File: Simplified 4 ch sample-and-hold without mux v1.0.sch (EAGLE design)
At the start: 8 parts, among them IC5 TL074JT

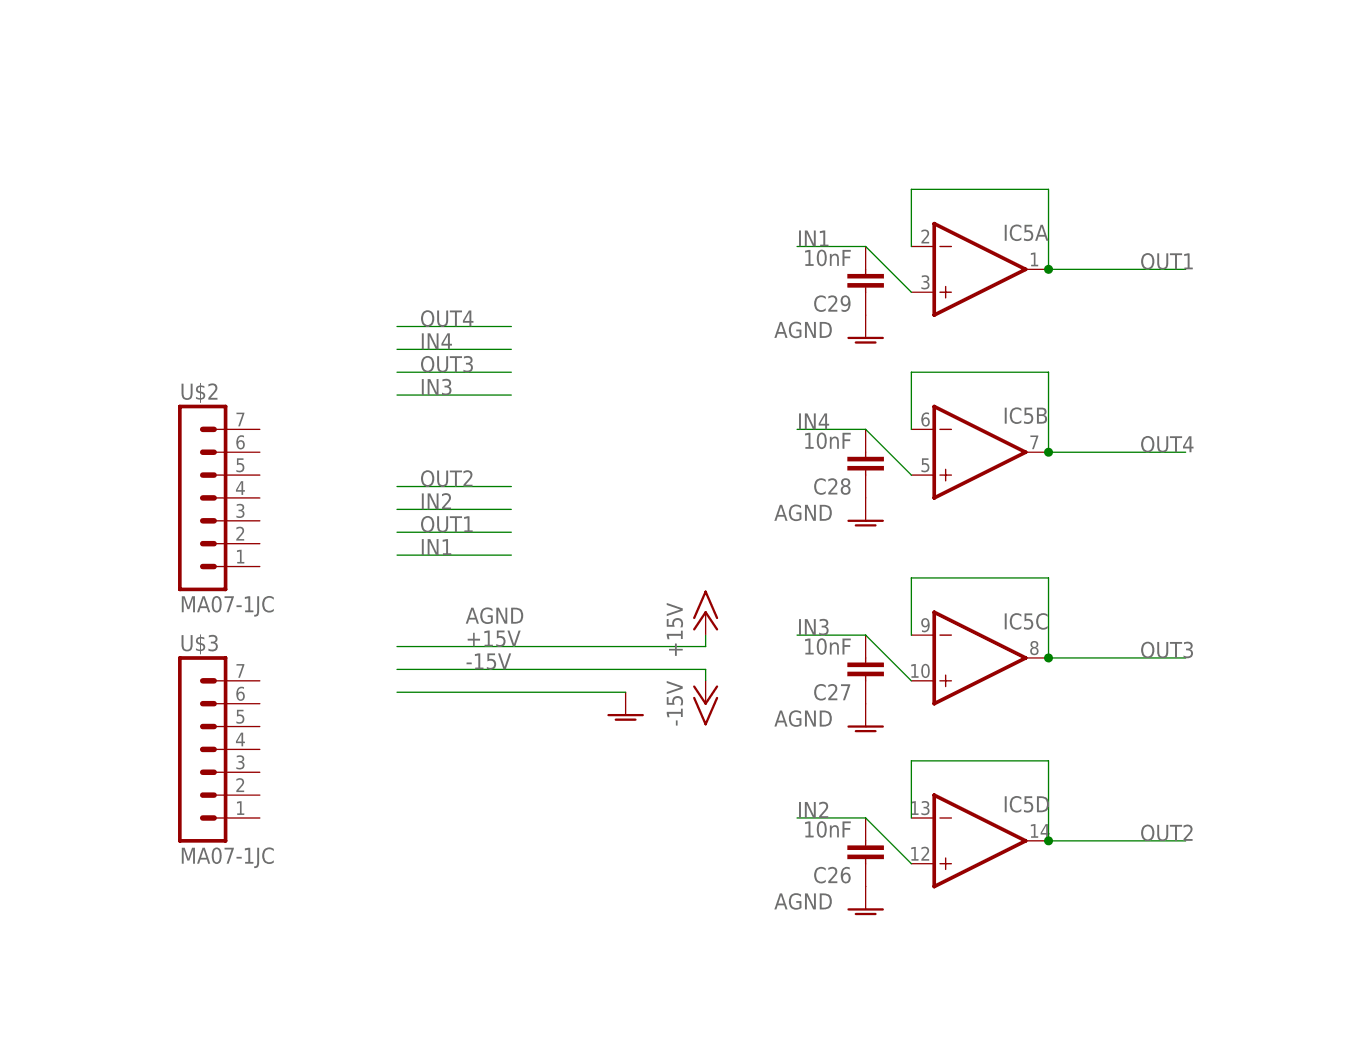
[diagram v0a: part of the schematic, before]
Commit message: Almost completed simplified 4ch s & h
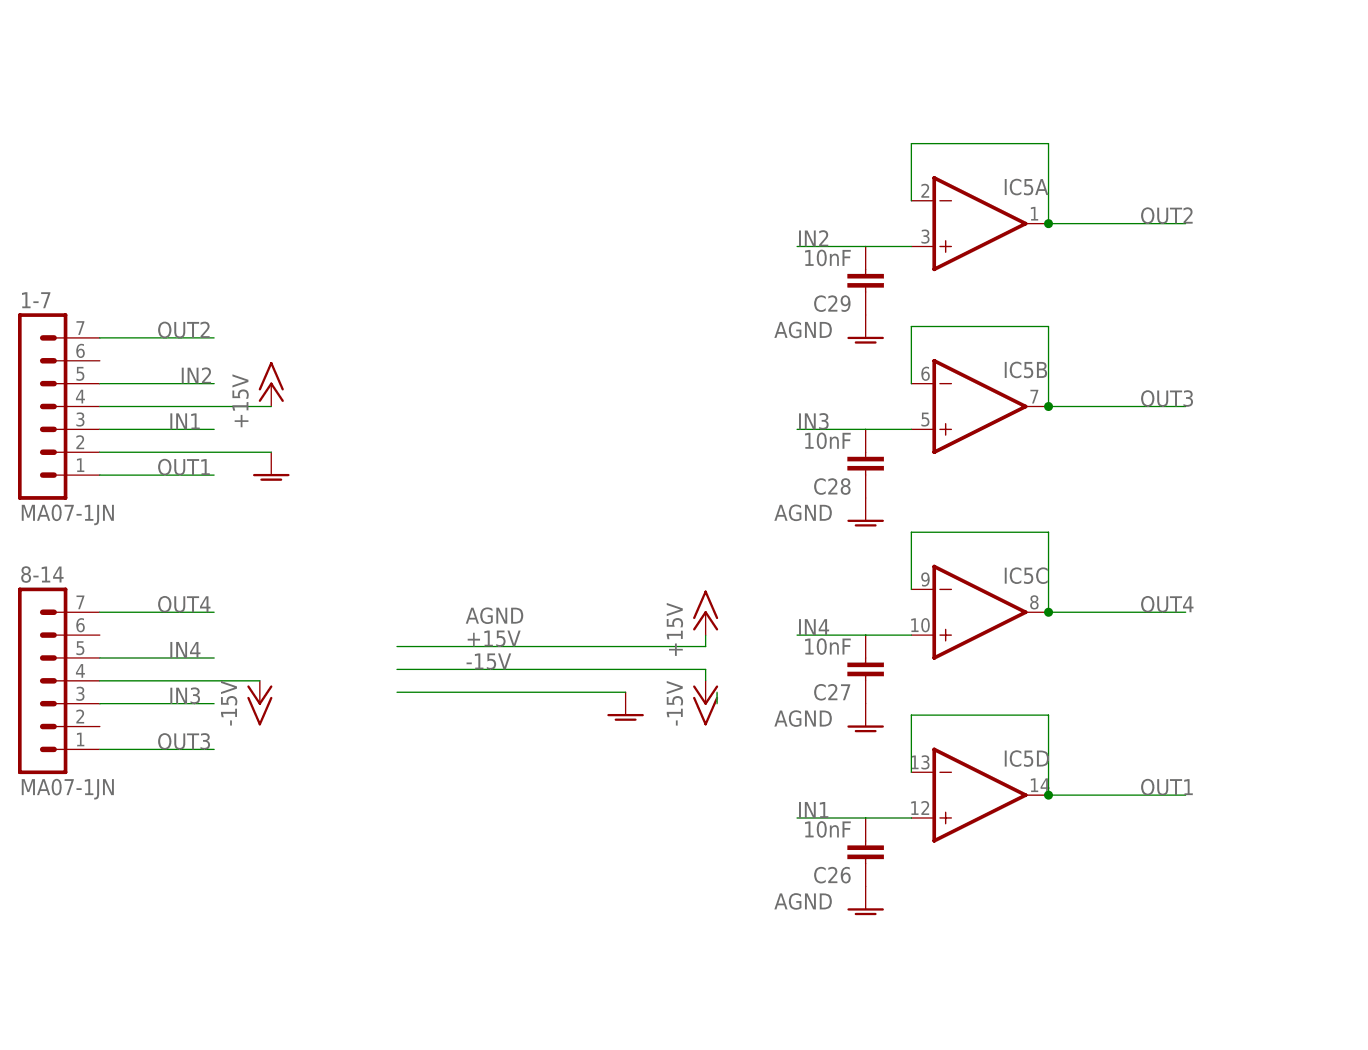
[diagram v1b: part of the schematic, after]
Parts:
- removed U$2, U$3: MA07-1JC, joakim:MA07-1JC
- added 1-7, 8-14: MA07-1JN, joakim:MA07-1JN
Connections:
- net +15V: now also 1-7.4
- net -15V: now also 8-14.4
- net AGND: now also 1-7.2
- net IN1: now also 1-7.3, C26.2, IC5D.+IN; no longer C29.2, IC5A.+IN
- net IN2: now also 1-7.5, C29.2, IC5A.+IN; no longer C26.2, IC5D.+IN
- net IN3: now also 8-14.3, C28.2, IC5B.+IN; no longer C27.2, IC5C.+IN
- net IN4: now also 8-14.5, C27.2, IC5C.+IN; no longer C28.2, IC5B.+IN
- net OUT1: now also 1-7.1, IC5D.-IN, IC5D.OUT; no longer IC5A.-IN, IC5A.OUT
- net OUT2: now also 1-7.7, IC5A.-IN, IC5A.OUT; no longer IC5D.-IN, IC5D.OUT
- net OUT3: now also 8-14.1, IC5B.-IN, IC5B.OUT; no longer IC5C.-IN, IC5C.OUT
- net OUT4: now also 8-14.7, IC5C.-IN, IC5C.OUT; no longer IC5B.-IN, IC5B.OUT
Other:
- moved on the sheet: IC5A, IC5B, IC5C, IC5D

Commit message: Fixed error in silk screen
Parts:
- IC5: value TL074JT -> TL084CPWR
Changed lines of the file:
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@@
 <setting verticaltext="up"/>
 </settings>
-<grid distance="0.05" unitdist="inch" unit="inch" style="lines" multiple="1" display="no" altdistance="0.01" altunitdist="inch" altunit="inch"/>
+<grid distance="0.1" unitdist="inch" unit="inch" style="lines" multiple="1" display="no" altdistance="0.01" altunitdist="inch" altunit="inch"/>
 <layers>
 <layer number="1" name="Top" color="4" fill="1" visible="no" active="no"/>
@@
 <part name="P+1" library="supply1" deviceset="+15V" device=""/>
 <part name="P-1" library="supply1" deviceset="-15V" device=""/>
-<part name="IC5" library="joakim" deviceset="TL074J" device="T"/>
+<part name="IC5" library="joakim" deviceset="TL074J" device="T" value="TL084CPWR"/>
 <part name="C29" library="rcl" library_urn="urn:adsk.eagle:library:334" deviceset="C-EU" device="C0805" package3d_urn="urn:adsk.eagle:package:23617/2" value="10nF"/>
 <part name="C28" library="rcl" library_urn="urn:adsk.eagle:library:334" deviceset="C-EU" device="C0805" package3d_urn="urn:adsk.eagle:package:23617/2" value="10nF"/>
